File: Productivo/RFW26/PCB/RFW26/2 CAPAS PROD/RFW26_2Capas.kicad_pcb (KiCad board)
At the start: 2 copper layers, 68.6 x 55.9 mm, 39 parts, among them J1 IN 12V, J10 OUT, J2 Receptor RF, J3 ESP01, J4 Conn_02x04_Counter_Clockwise, J6 Receptor RF, J9 jumpers salida, K2 SANYOU_SRD_Form_C, Q2 MMBT5551L, SW1 RESET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

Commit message: RFW26 1 capa
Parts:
- removed J6: Receptor RF, Connector_PinSocket_2.54mm:PinSocket_1x04_P2.54mm_Vertical
- added ANT1: ANT, Connector_PinSocket_2.54mm:PinSocket_1x01_P2.54mm_Vertical, F.Cu at (83.9, 125.1)
- added C6: 0.1u, Capacitor_SMD:C_1206_3216Metric_Pad1.33x1.80mm_HandSolder, F.Cu at (139.1, 134.0)
- added J5: Receptor RF, Connector_PinSocket_2.54mm:PinSocket_1x04_P2.54mm_Vertical, F.Cu at (89.6, 125.1)
- D4, D5: footprint Diode_SMD:D_SMC_Handsoldering -> Kicad Modelos:SS34B-HF
- U1: footprint Package_TO_SOT_THT:TO-220-5_Vertical -> Kicad Modelos:LM2596TVADJG
- U2: footprint Package_TO_SOT_SMD:SOT-223-3_TabPin2 -> Kicad Modelos:TLV1117LV33DCYR
- moved J2 35.0 mm to (130.3, 125.1)
- moved D2 27.1 mm to (120.7, 172.4), turned to 180 degrees
- moved R6 13.2 mm to (100.0, 145.4)
- moved D7 9.37 mm to (89.5, 131.5), turned to 90 degrees
- moved R5 7.61 mm to (93.7, 145.4)
- moved R11 6.26 mm to (89.5, 136.9), turned to -90 degrees
- moved R1 5.53 mm to (88.9, 157.8)
- moved U1 5.08 mm to (94.0, 132.1)
- moved R9 4.59 mm to (134.6, 133.9)
- moved J10 4.53 mm to (102.2, 172.7)
- moved J9 4.52 mm to (102.2, 165.1)
- moved R2 4.39 mm to (92.7, 157.8)
- moved D5 4.30 mm to (80.7, 158.0)
- moved R4 3.42 mm to (96.5, 157.8)
- moved SW1 2.57 mm to (125.7, 172.4)
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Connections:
- J2 pad 4: +5V -> unconnected-(J2-Pin_4-Pad4)
- W26/34 pad 1: D1 -> GND
- W26/34 pad 2: D0 -> D1
- W26/34 pad 3: GND -> D0
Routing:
- net Net-(J2-Pin_2): track 62.6 -> 36.1 mm, vias 1 -> 0
- net GND: track 282.2 -> 257.1 mm, vias 3 -> 2
- net Net-(J3-Pin_5): track 39.1 -> 61.5 mm, vias 0 -> 2
- net Net-(D2-A): track 12.4 -> 30.2 mm, vias 0 -> 1
- net Net-(J3-Pin_4): track 32.4 -> 43.2 mm, vias 0 -> 3
- net +5V: track 131.2 -> 140.8 mm
- net 12V: track 74.2 -> 83.7 mm, vias 0 -> 2
- net Net-(D1-A): track 19.8 -> 29.0 mm
- net D0: track 39.7 -> 48.0 mm, vias 1 -> 3
- net Net-(U1-FB): track 10.7 -> 18.6 mm
- net +3.3V: track 72.2 -> 79.1 mm, vias 1 -> 2
- net Net-(D6-K): track 90.9 -> 97.6 mm
- net Net-(ANT1-Pin_1): track 0.00 -> 5.74 mm
- net 12VOUT: track 30.7 -> 35.5 mm
- net Net-(J10-Pin_2): track 18.9 -> 23.5 mm, vias 0 -> 1
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
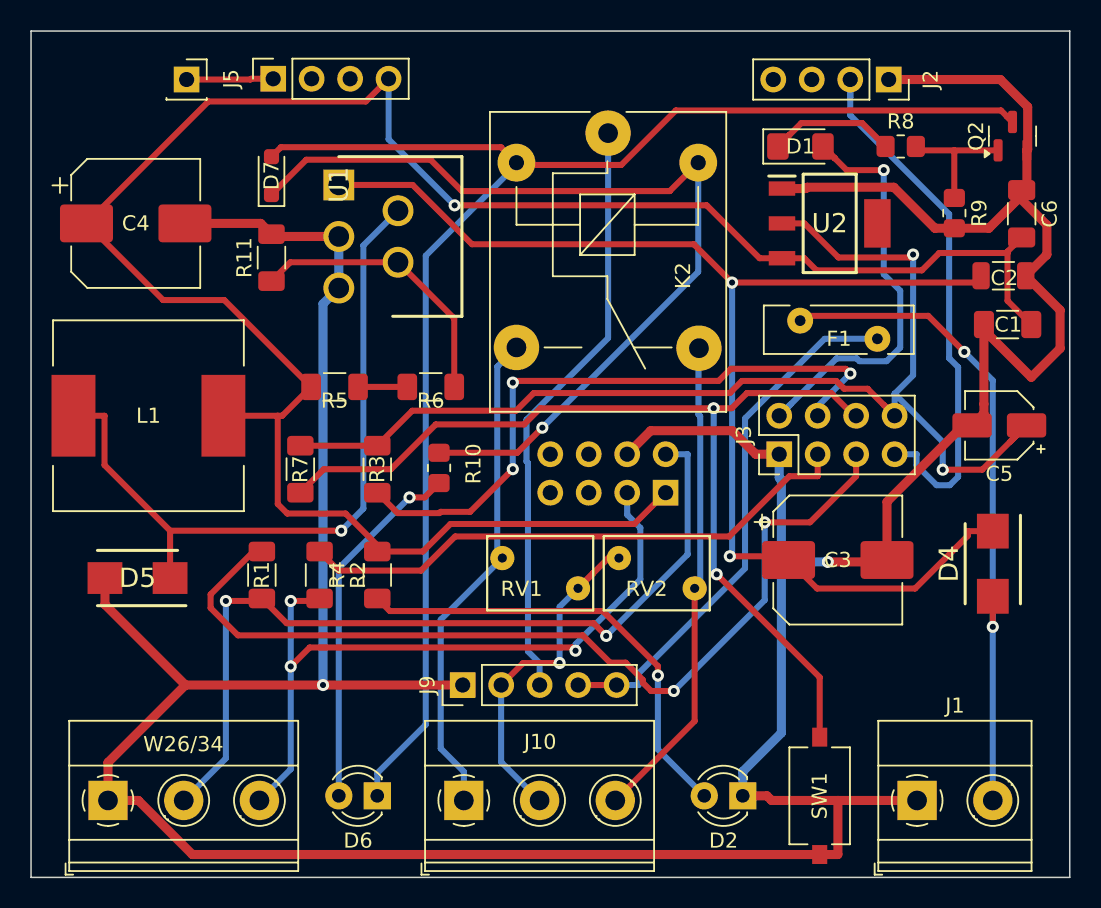
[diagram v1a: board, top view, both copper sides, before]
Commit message: Update PCB design parameters and remove temporary lock file
- Increased clearance from 0.4 to 0.5 for improved signal integrity.
- Adjusted track width from 0.4 to 0.5 and via diameter from 0.8 to 2.0 for better manufacturability.
- Removed unnecessary lock file for antenna frequency spreadsheet.
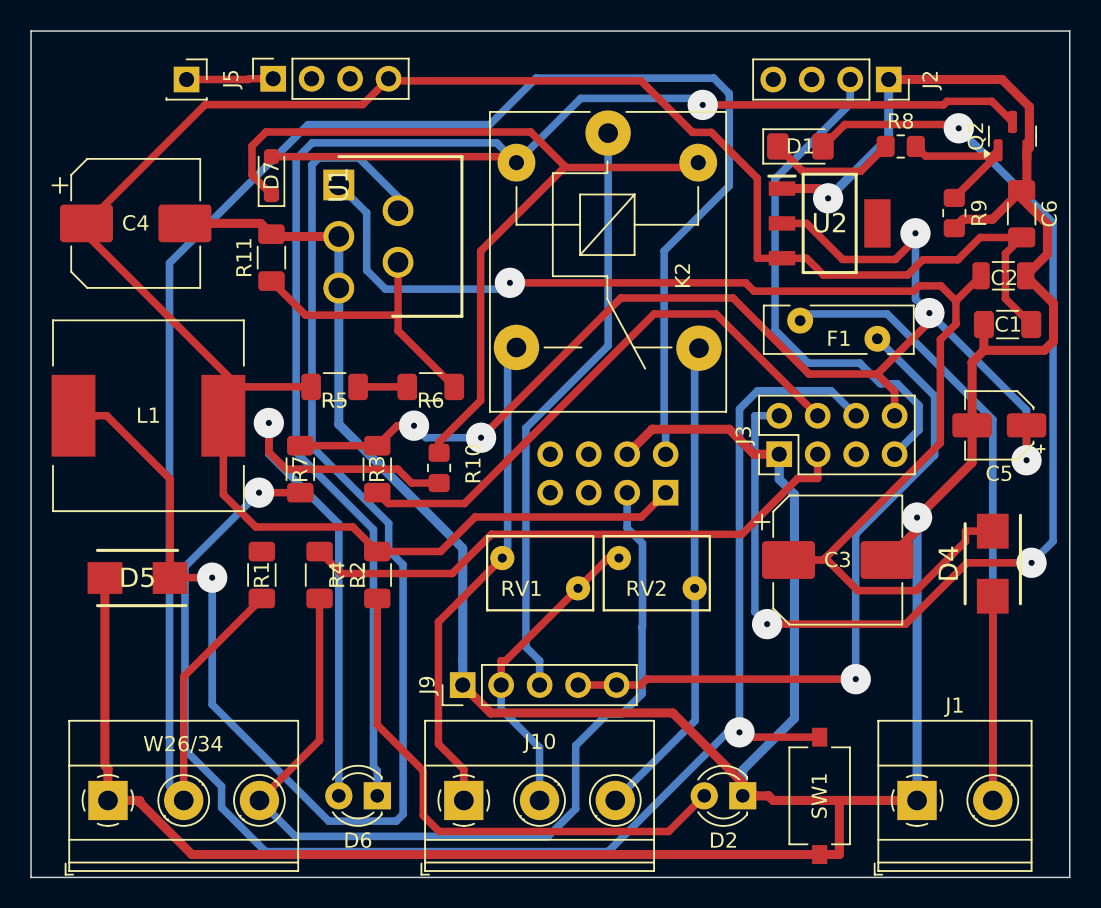
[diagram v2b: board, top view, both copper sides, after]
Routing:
- net D1: track 56.2 -> 119.4 mm, vias 2 -> 0
- net Net-(J3-Pin_5): track 61.5 -> 0.00 mm, vias 2 -> 0
- net Net-(D1-A): track 29.0 -> 76.4 mm, vias 1 -> 3
- net Net-(D5-K): track 48.5 -> 95.0 mm
- net Net-(J3-Pin_6): track 64.7 -> 100.9 mm
- net Net-(D6-A): track 24.0 -> 40.5 mm
- net Net-(D6-K): track 97.6 -> 111.5 mm, vias 0 -> 1
- net D0: track 48.0 -> 61.3 mm, vias 3 -> 0
- net GND: track 257.1 -> 269.1 mm
- net Net-(D4-A): track 44.4 -> 54.4 mm, vias 2 -> 0
- net 12VOUT: track 35.5 -> 44.7 mm, vias 0 -> 1
- net Net-(J3-Pin_4): track 43.2 -> 37.3 mm, vias 3 -> 0
- net +3.3V: track 79.1 -> 84.6 mm, vias 2 -> 5
- net Net-(D2-A): track 30.2 -> 35.6 mm, vias 1 -> 0
- net Net-(D7-K): track 60.0 -> 57.0 mm, vias 1 -> 0
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
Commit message: Actualizacion de RFW26 a tamaño 80x45
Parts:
- removed J1: IN 12V, TerminalBlock_Phoenix:TerminalBlock_Phoenix_MKDS-1,5-2_1x02_P5.00mm_Horizontal
- removed W26/34: Screw_Terminal_01x03, TerminalBlock_Phoenix:TerminalBlock_Phoenix_MKDS-1,5-3_1x03_P5.00mm_Horizontal
- added W26/34-12+1: Screw_Terminal_01x04, TerminalBlock_Phoenix:TerminalBlock_Phoenix_MKDS-1,5-4_1x04_P5.00mm_Horizontal, F.Cu at (109.2, 92.7)
- moved D6 92.7 mm to (147.8, 95.2)
- moved J9 84.1 mm to (137.7, 88.9)
- moved J10 80.5 mm to (93.4, 92.7)
- moved SW1 79.8 mm to (131.3, 92.8), turned to -90 degrees
- moved D2 79.6 mm to (140.2, 95.2)
- moved ANT1 67.7 mm to (95.9, 58.4)
- moved J2 67.7 mm to (142.2, 58.4)
- moved J5 67.7 mm to (101.6, 58.4)
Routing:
- net GND: track 269.1 -> 0.00 mm, vias 2 -> 0
- net +5V: track 141.8 -> 0.00 mm
- net D1: track 119.4 -> 0.00 mm
- net Net-(D6-K): track 111.5 -> 0.00 mm, vias 1 -> 0
- net Net-(J3-Pin_6): track 100.9 -> 0.00 mm, vias 2 -> 0
- net Net-(D5-K): track 95.0 -> 0.00 mm, vias 1 -> 0
- net 12V: track 86.1 -> 0.00 mm, vias 1 -> 0
- net +3.3V: track 84.6 -> 0.00 mm, vias 5 -> 0
- net Net-(D1-A): track 76.4 -> 0.00 mm, vias 3 -> 0
- net D0: track 61.3 -> 0.00 mm
- net Net-(D7-K): track 57.0 -> 0.00 mm
- net Net-(D4-A): track 54.4 -> 0.00 mm
- net 12VOUT: track 44.7 -> 0.00 mm, vias 1 -> 0
- net Net-(D6-A): track 40.5 -> 0.00 mm, vias 1 -> 0
- net Net-(J9-Pin_3): track 39.1 -> 0.00 mm
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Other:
- board size 68.6 x 55.9 mm -> 80 x 45 mm

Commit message: RFW26 2 capa 45x80
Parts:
- moved C3 99.4 mm to (153.1, 61.0), turned to 180 degrees
- moved J4 91.9 mm to (124.5, 61.0)
- moved R1 86.1 mm to (133.3, 84.1)
- moved L1 79.7 mm to (100.3, 69.8)
- moved R2 79.3 mm to (121.9, 84.1)
- moved R10 76.1 mm to (155.2, 97.8), turned to 0 degrees
- moved R4 75.6 mm to (113.0, 84.1)
- moved R3 74.5 mm to (129.5, 84.1), turned to 90 degrees
- moved C4 72.6 mm to (87.0, 62.3), turned to -90 degrees
- moved C5 72.4 mm to (136.6, 75.6)
- moved RV2 72.1 mm to (105.0, 85.0), turned to 90 degrees
- moved R7 71.6 mm to (117.5, 84.1)
- moved RV1 71.5 mm to (95.9, 85.7), turned to 90 degrees
- moved D1 70.1 mm to (130.0, 59.7), turned to -90 degrees
- moved D4 69.8 mm to (155.6, 89.8)
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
